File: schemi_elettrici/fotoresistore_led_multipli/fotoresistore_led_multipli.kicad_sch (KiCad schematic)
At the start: 11 parts

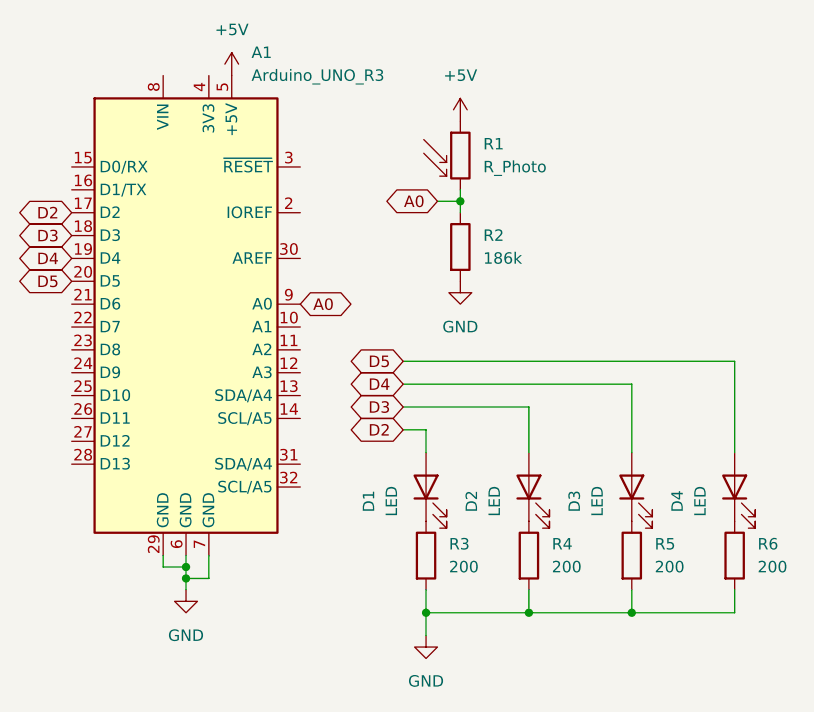
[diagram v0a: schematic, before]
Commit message: rimozione led in piu`
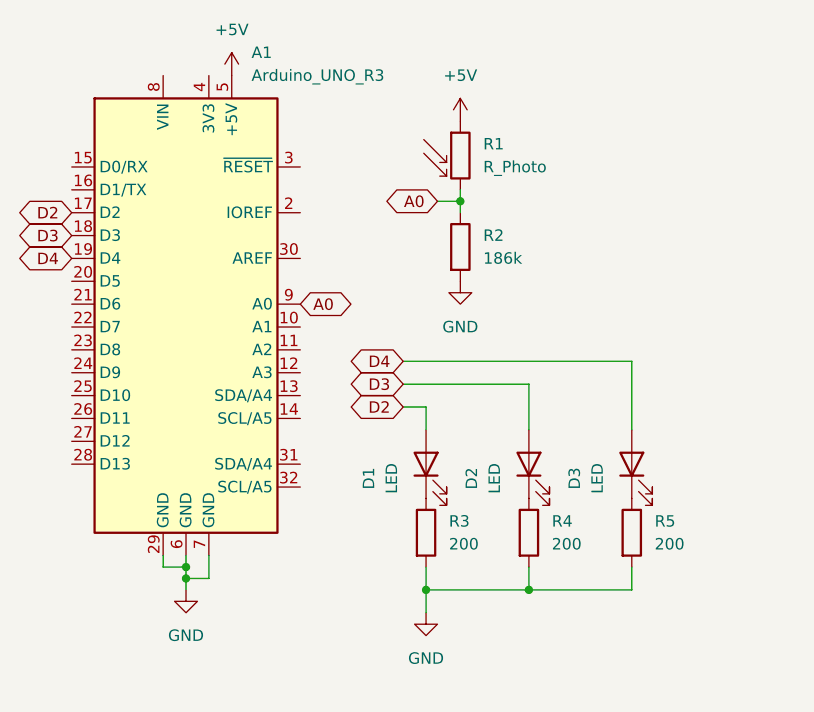
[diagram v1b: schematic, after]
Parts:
- removed D4: LED, symbol Device:LED
- removed R6: 200, symbol Device:R
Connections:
- net D5: no longer names the net of A1.20 (D5)
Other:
- moved on the sheet: D1, D2, D3, R3, R4, R5
